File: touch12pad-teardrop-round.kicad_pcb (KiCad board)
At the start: 2 copper layers, 158.8 x 33.2 mm, 38 parts, among them J1 Conn_01x01_Female, J10 Conn_01x01_Female, J11 Conn_01x01_Female, J12 Conn_01x01_Female, J13 Conn_01x01_Female, J14 Conn_01x01_Female, J15 Conn_01x01_Female, J16 Conn_01x01_Female, J17 Conn_01x01_Female, J18 Conn_01x01_Female, J19 Conn_01x01_Female, J2 Conn_01x01_Female, J20 Conn_01x01_Female, J21 Conn_01x01_Female, J22 Conn_01x01_Female, J23 Conn_01x01_Female, J24 Conn_01x01_Female, J3 Conn_01x01_Female, J4 \, J5 Conn_01x01_Female, J6 Conn_01x01_Female, J7 Conn_01x01_Female, J8 Conn_01x01_Female, J9 Conn_01x01_Female

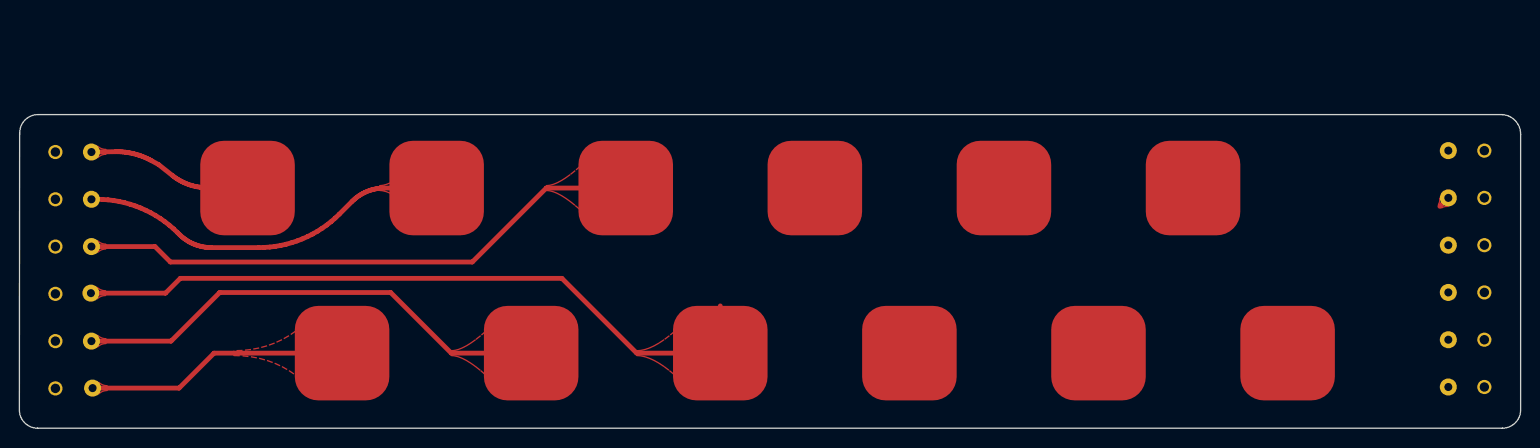
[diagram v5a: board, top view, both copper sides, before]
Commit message: final version of flextouch with round tracks
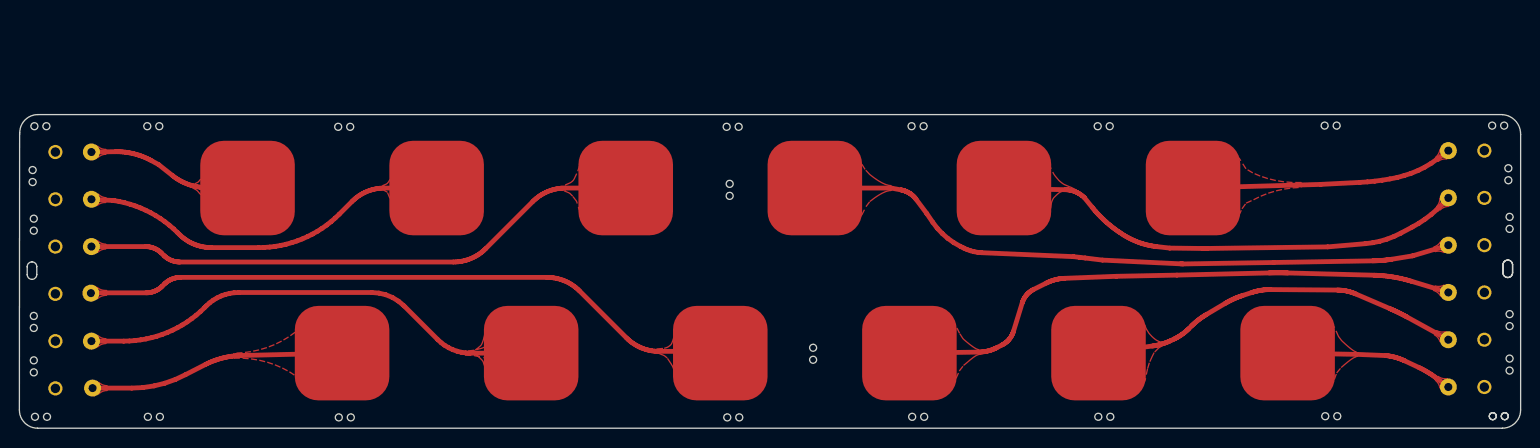
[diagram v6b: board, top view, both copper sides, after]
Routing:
- net Net-(J18-Pad1): track 0.00 -> 70.1 mm
- net Net-(J15-Pad1): track 0.00 -> 61.3 mm
- net Net-(J17-Pad1): track 1.27 -> 50.8 mm
- net Net-(J14-Pad1): track 0.00 -> 39.9 mm
- net Net-(J16-Pad1): track 0.00 -> 27.8 mm
- net Net-(J13-Pad1): track 0.00 -> 17.9 mm
- net Net-(J12-Pad1): track 75.5 -> 69.6 mm
- net Net-(J11-Pad1): track 51.3 -> 50.1 mm
- net Net-(J10-Pad1): track 27.9 -> 27.0 mm
- net Net-(J9-Pad1): track 60.4 -> 59.8 mm
- net Net-(J8-Pad1): track 39.8 -> 40.4 mm
- added copper zone on F.Cu, net Net-(J1-Pad1)
- added copper zone on F.Cu, net Net-(J11-Pad1)
- added copper zone on F.Cu, net Net-(J12-Pad1)
- added copper zone on F.Cu, net Net-(J14-Pad1)
- added copper zone on F.Cu, net Net-(J17-Pad1)
- added copper zone on F.Cu, net Net-(J8-Pad1)
- added copper zone on F.Cu, net Net-(J9-Pad1)
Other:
- outline, holes or cut-outs redrawn
- board text added: "Flex Touch Band [2020-01-03] @HelenLeigh + Drew (@pdp7) github.com/helenleigh/flextouch"
- board text removed: "Flex Touch Band [2019-12-21] @HelenLeigh + Drew (@pdp7) github.com/helenleigh/flextouch"
